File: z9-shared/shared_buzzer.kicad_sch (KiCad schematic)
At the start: 6 parts, among them Q701 AO3400A

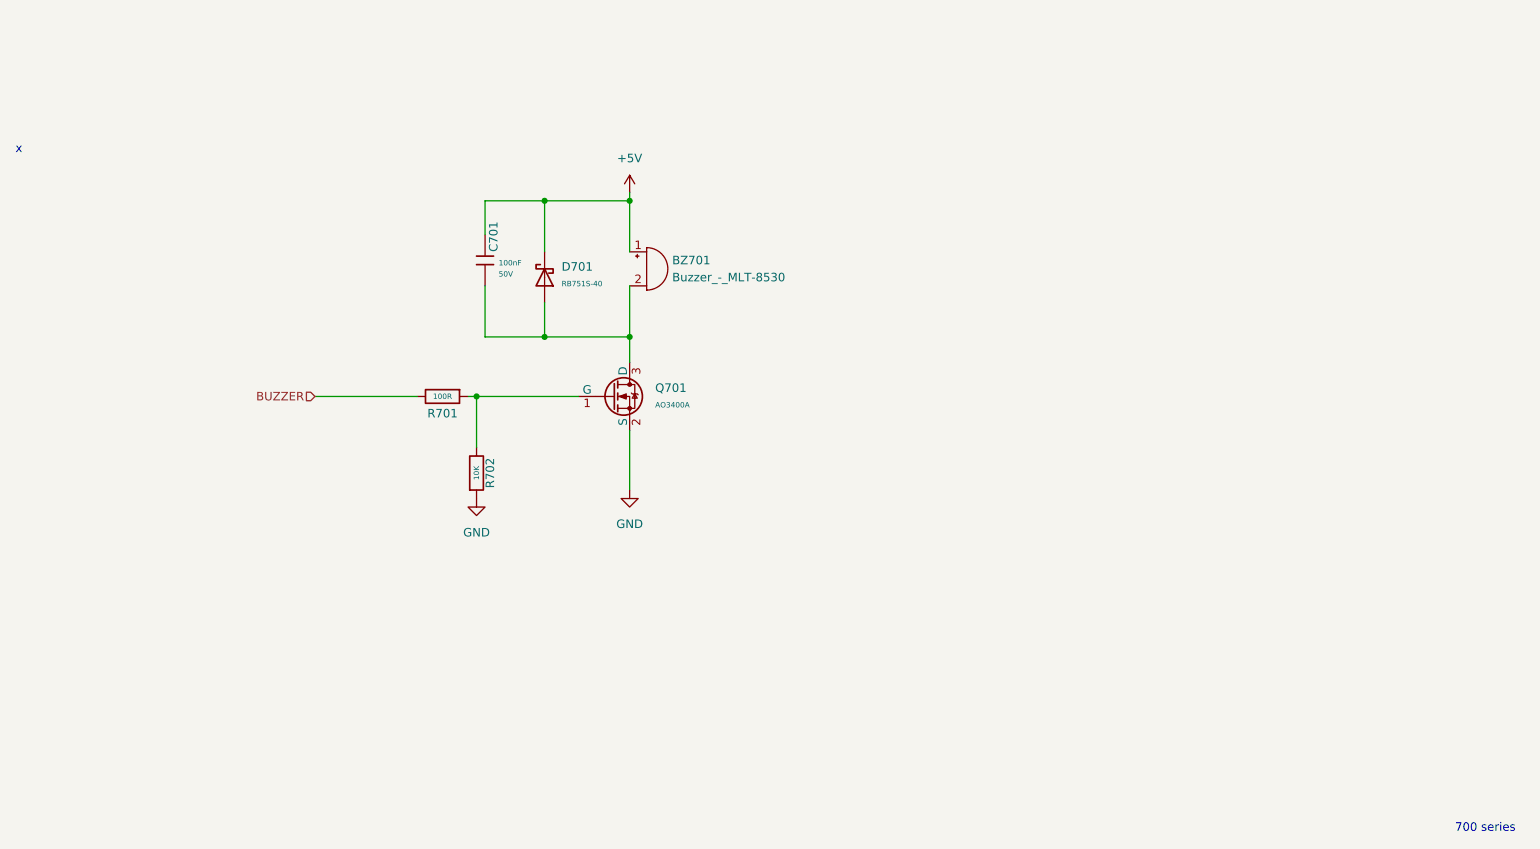
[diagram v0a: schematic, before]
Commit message: Add shared_ism330dhcx schematic and update project configuration - Buzzer chaNGES 3.3v BEADS ANDCAPS - Created a new schematic file for the shared_ism330dhcx component. - Updated the z9-shared project configuration to change the annotation start number from 950 to 700. - Added the shared_ism330dhcx sheet to the main schematic with relevant properties and instances.
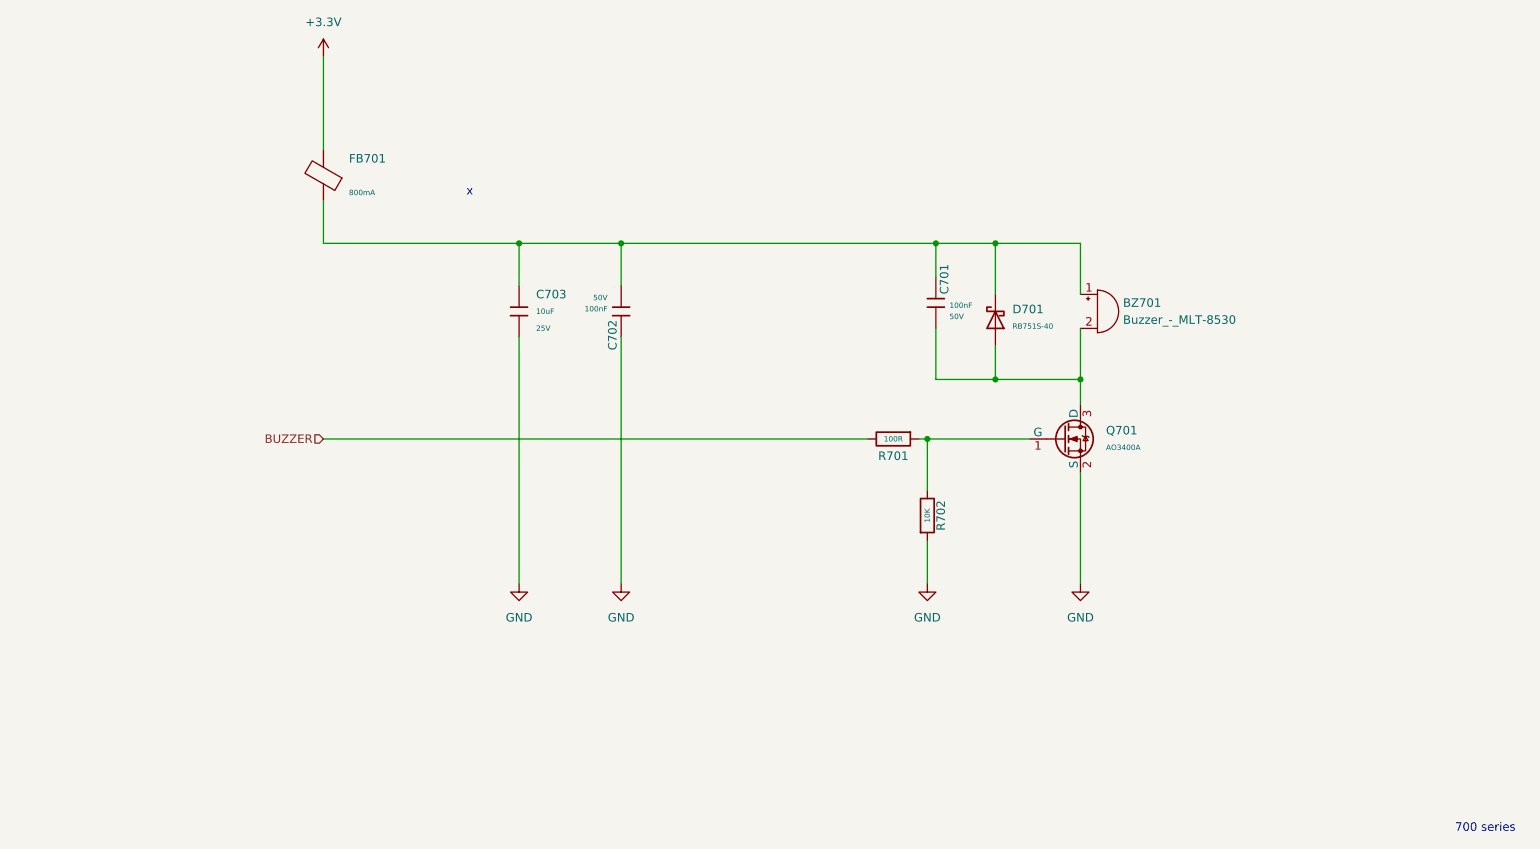
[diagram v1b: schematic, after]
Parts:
- added C702: 100nF, dnt:C_0603_1608Metric, symbol dnt_global:0603,100nF
- added C703: 10uF, dnt:C_0603_1608Metric, symbol dnt_global:0603,10uF,_25V
- added FB701: ~, PCM_JLCPCB:FB_0805, symbol PCM_JLCPCB-Inductors:Ferrite,0805
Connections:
- net GND: now also C702.1, C703.2
- net +5V: no longer names the net of BZ701.1 (+), C701.1, D701.1
- net +5V: now also C702.2, C703.1, FB701.1
- new net +3.3V: FB701.2
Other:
- moved on the sheet: BZ701, C701, D701, Q701, R701, R702

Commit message: fix footprint
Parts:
- FB701: footprint PCM_JLCPCB:FB_0805 -> dnt:F_0805_2012Metric; symbol PCM_JLCPCB-Inductors:Ferrite,0805 -> dnt_global:Ferrite,0805_800mA
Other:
- note removed: "x"
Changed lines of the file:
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@@
 		(comment 1 "Some schematic is shared ")
-	)
-	(text "x"
-		(exclude_from_sim no)
-		(at 125.984 68.58 0)
-		(effects
-			(font
-				(size 1.27 1.27)
-			)
-		)
 	)
 	(text "700 series "
@@
 	)
 	(symbol
-		(lib_id "PCM_JLCPCB-Inductors:Ferrite,0805")
+		(lib_id "dnt_global:Ferrite,0805_800mA")
 		(at 104.14 66.04 180)
 		(unit 1)
@@
 		(fields_autoplaced yes)
 		(property "Reference" "FB701"
-			(at 107.95 63.5507 0)
+			(at 107.95 64.8207 0)
 			(effects
 				(font
@@
 		)
 		(property "Value" "~"
-			(at 107.95 66.0908 0)
+			(at 104.14 66.04 0)
 			(effects
 				(font
 					(size 0.8 0.8)
 				)
-				(justify right)
-			)
-		)
-		(property "Footprint" "PCM_JLCPCB:FB_0805"
+				(justify left)
+			)
+		)
+		(property "Footprint" "dnt:F_0805_2012Metric"
 			(at 105.918 66.04 90)
 			(effects
@@
 		)
 		(property "Current Rating" "800mA"
-			(at 107.95 68.6308 0)
-			(effects
-				(font
+			(at 107.95 67.3608 0)
+			(effects
+				(font

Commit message: Update schematic and project settings for shared components
- Changed the starting annotation number from 700 to 975 in the project configuration.
- Added a new shared schematic sheet named "shared_isolated_can_ps" with relevant properties and instances.
- Included a cautionary text in the schematic to avoid moving components and reannotating to prevent loss of links.
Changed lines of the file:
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@@
 		(fields_autoplaced yes)
 		(property "Reference" "FB701"
-			(at 107.95 64.8207 0)
+			(at 107.95 63.5507 0)
 			(effects
 				(font
@@
 		)
 		(property "Value" "~"
-			(at 104.14 66.04 0)
+			(at 107.95 66.0908 0)
 			(effects
 				(font
 					(size 0.8 0.8)
 				)
-				(justify left)
+				(justify right)
 			)
 		)
@@
 		)
 		(property "Current Rating" "800mA"
-			(at 107.95 67.3608 0)
+			(at 107.95 68.6308 0)
 			(effects
 				(font
@@
 				(path "/09e08bdc-786f-4949-8afc-e02ddbe0502e/1a1ef1d0-80f8-40e1-820b-d8a0de9a6f67"
 					(reference "FB701")
+					(unit 1)
+				)
+			)
+			(project "z9-console"
+				(path "/8d063f79-9282-4820-bcf4-1ff3c006cf08/8d0cf1ff-dd45-490a-9f6d-ad4eb4a5c201"
+					(reference "FB?")
 					(unit 1)
 				)
@@
 				)
 			)
+			(project "z9-console"
+				(path "/8d063f79-9282-4820-bcf4-1ff3c006cf08/8d0cf1ff-dd45-490a-9f6d-ad4eb4a5c201"
+					(reference "#PWR0101")
+					(unit 1)
+				)
+			)
 		)
 	)
@@
 				)
 			)
+			(project "z9-console"
+				(path "/8d063f79-9282-4820-bcf4-1ff3c006cf08/8d0cf1ff-dd45-490a-9f6d-ad4eb4a5c201"
+					(reference "C?")
+					(unit 1)
+				)
+			)
 		)
 	)
@@
 				)
 			)
+			(project "z9-console"
+				(path "/8d063f79-9282-4820-bcf4-1ff3c006cf08/8d0cf1ff-dd45-490a-9f6d-ad4eb4a5c201"
+					(reference "#PWR0102")
+					(unit 1)
+				)
+			)
 		)
 	)
@@
 				)
 			)
+			(project "z9-console"
+				(path "/8d063f79-9282-4820-bcf4-1ff3c006cf08/8d0cf1ff-dd45-490a-9f6d-ad4eb4a5c201"
+					(reference "C?")
+					(unit 1)
+				)
+			)
 		)
 	)
@@
 					(unit 1)
 				)
+			)
+			(project "z9-console"
+				(path "/8d063f79-9282-4820-bcf4-1ff3c006cf08/8d0cf1ff-dd45-490a-9f6d-ad4eb4a5c201"
+					(reference "#PWR0103")
+					(unit 1)
+				)

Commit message: Add z9-console project references and update component properties in shared_buzzer schematic
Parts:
- renumbered C703 to C701, C701 to C703
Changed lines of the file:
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@@
+				)
+			)
+			(project "z9-console"
+				(path "/8d063f79-9282-4820-bcf4-1ff3c006cf08/f06e6e31-c68d-491a-ad1f-dc0bf57e1d1a"
+					(reference "Q701")
+					(unit 1)
 				)
 			)
@@
 				)
 			)
+			(project "z9-console"
+				(path "/8d063f79-9282-4820-bcf4-1ff3c006cf08/f06e6e31-c68d-491a-ad1f-dc0bf57e1d1a"
+					(reference "D701")
+					(unit 1)
+				)
+			)
 			(project "z9-pdm"
 				(path "/b643db5c-578e-4b48-aafc-cc4190db582a/c97401c5-7e03-4d93-a14f-f692468677b5"
@@
 		(dnp no)
 		(fields_autoplaced yes)
-		(property "Reference" "#PWR0704"
+		(property "Reference" "#PWR0702"
 			(at 133.35 133.35 0)
 			(effects
@@
 				(path "/09e08bdc-786f-4949-8afc-e02ddbe0502e/1a1ef1d0-80f8-40e1-820b-d8a0de9a6f67"
 					(reference "#PWR0704")
+					(unit 1)
+				)
+			)
+			(project "z9-console"
+				(path "/8d063f79-9282-4820-bcf4-1ff3c006cf08/f06e6e31-c68d-491a-ad1f-dc0bf57e1d1a"
+					(reference "#PWR0702")
 					(unit 1)
 				)
@@
 		(dnp no)
 		(fields_autoplaced yes)
-		(property "Reference" "#PWR0701"
+		(property "Reference" "#PWR0704"
 			(at 194.31 133.35 0)
 			(effects
@@
 				(path "/09e08bdc-786f-4949-8afc-e02ddbe0502e/1a1ef1d0-80f8-40e1-820b-d8a0de9a6f67"
 					(reference "#PWR0701")
+					(unit 1)
+				)
+			)
+			(project "z9-console"
+				(path "/8d063f79-9282-4820-bcf4-1ff3c006cf08/f06e6e31-c68d-491a-ad1f-dc0bf57e1d1a"
+					(reference "#PWR0704")
 					(unit 1)
 				)
@@
 				)
 			)
+			(project "z9-console"
+				(path "/8d063f79-9282-4820-bcf4-1ff3c006cf08/f06e6e31-c68d-491a-ad1f-dc0bf57e1d1a"
+					(reference "C702")
+					(unit 1)
+				)
+			)
 		)
 	)
@@
 		(on_board yes)
 		(dnp no)
-		(property "Reference" "C701"
+		(property "Reference" "C703"
 			(at 196.85 83.82 90)
 			(effects
@@
 				(path "/09e08bdc-786f-4949-8afc-e02ddbe0502e/1a1ef1d0-80f8-40e1-820b-d8a0de9a6f67"
 					(reference "C701")
+					(unit 1)
+				)
+			)
+			(project "z9-console"
+				(path "/8d063f79-9282-4820-bcf4-1ff3c006cf08/f06e6e31-c68d-491a-ad1f-dc0bf57e1d1a"
+					(reference "C703")
 					(unit 1)
 				)
@@
 				)
 			)
+			(project "z9-console"
+				(path "/8d063f79-9282-4820-bcf4-1ff3c006cf08/f06e6e31-c68d-491a-ad1f-dc0bf57e1d1a"
+					(reference "BZ701")
+					(unit 1)
+				)
+			)
 			(project "z9-pdm"
 				(path "/b643db5c-578e-4b48-aafc-cc4190db582a/c97401c5-7e03-4d93-a14f-f692468677b5"
@@
 		(dnp no)
 		(fields_autoplaced yes)
-		(property "Reference" "#PWR0702"
+		(property "Reference" "#PWR0703"
 			(at 148.59 133.35 0)
 			(effects
@@
 				(path "/09e08bdc-786f-4949-8afc-e02ddbe0502e/1a1ef1d0-80f8-40e1-820b-d8a0de9a6f67"
 					(reference "#PWR0702")
+					(unit 1)
+				)
+			)
+			(project "z9-console"
+				(path "/8d063f79-9282-4820-bcf4-1ff3c006cf08/f06e6e31-c68d-491a-ad1f-dc0bf57e1d1a"
+					(reference "#PWR0703")
 					(unit 1)
 				)
@@
 		(dnp no)
 		(fields_autoplaced yes)
-		(property "Reference" "C703"
+		(property "Reference" "C701"
 			(at 135.89 83.8199 0)
 			(effects
@@
 			(project ""
 				(path "/8d063f79-9282-4820-bcf4-1ff3c006cf08/f06e6e31-c68d-491a-ad1f-dc0bf57e1d1a"
-					(reference "C703")
+					(reference "C701")
 					(unit 1)
 				)
@@
 				)
 			)
+			(project "z9-console"
+				(path "/8d063f79-9282-4820-bcf4-1ff3c006cf08/f06e6e31-c68d-491a-ad1f-dc0bf57e1d1a"
+					(reference "R702")
+					(unit 1)
+				)
+			)
 			(project "z9-pdm"
 				(path "/b643db5c-578e-4b48-aafc-cc4190db582a/c97401c5-7e03-4d93-a14f-f692468677b5"
@@
 		(dnp no)
 		(fields_autoplaced yes)
-		(property "Reference" "#PWR0953"
+		(property "Reference" "#PWR0701"
 			(at 104.14 52.07 0)
 			(effects
@@
 			(project ""
 				(path "/8d063f79-9282-4820-bcf4-1ff3c006cf08/f06e6e31-c68d-491a-ad1f-dc0bf57e1d1a"
-					(reference "#PWR0953")
+					(reference "#PWR0701")
 					(unit 1)
 				)
@@
 				)
 			)
+			(project "z9-console"
+				(path "/8d063f79-9282-4820-bcf4-1ff3c006cf08/f06e6e31-c68d-491a-ad1f-dc0bf57e1d1a"
+					(reference "R701")
+					(unit 1)
+				)
+			)
 			(project "z9-pdm"
 				(path "/b643db5c-578e-4b48-aafc-cc4190db582a/c97401c5-7e03-4d93-a14f-f692468677b5"
@@
 		(dnp no)
 		(fields_autoplaced yes)
-		(property "Reference" "#PWR0703"
+		(property "Reference" "#PWR0705"
 			(at 217.17 133.35 0)
 			(effects
@@
 					(unit 1)
 				)
+			)
+			(project "z9-console"
+				(path "/8d063f79-9282-4820-bcf4-1ff3c006cf08/f06e6e31-c68d-491a-ad1f-dc0bf57e1d1a"
+					(reference "#PWR0705")
+					(unit 1)
+				)

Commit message: x
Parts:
- renumbered C703 to C701, C701 to C703
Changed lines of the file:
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@@
 		(instances
 			(project ""
-				(path "/09e08bdc-786f-4949-8afc-e02ddbe0502e/1a1ef1d0-80f8-40e1-820b-d8a0de9a6f67"
+				(path "/09e08bdc-786f-4949-8afc-e02ddbe0502e/4ba7270b-fda7-4f09-aaf0-2021d0ea5e88"
 					(reference "FB701")
 					(unit 1)
@@
 		(instances
 			(project "z9-shared"
-				(path "/09e08bdc-786f-4949-8afc-e02ddbe0502e/1a1ef1d0-80f8-40e1-820b-d8a0de9a6f67"
+				(path "/09e08bdc-786f-4949-8afc-e02ddbe0502e/4ba7270b-fda7-4f09-aaf0-2021d0ea5e88"
 					(reference "Q701")
 					(unit 1)
@@
 		(instances
 			(project "z9-shared"
-				(path "/09e08bdc-786f-4949-8afc-e02ddbe0502e/1a1ef1d0-80f8-40e1-820b-d8a0de9a6f67"
+				(path "/09e08bdc-786f-4949-8afc-e02ddbe0502e/4ba7270b-fda7-4f09-aaf0-2021d0ea5e88"
 					(reference "D701")
 					(unit 1)
@@
 		(dnp no)
 		(fields_autoplaced yes)
-		(property "Reference" "#PWR0702"
+		(property "Reference" "#PWR0704"
 			(at 133.35 133.35 0)
 			(effects
@@
 		(instances
 			(project "z9-shared"
-				(path "/09e08bdc-786f-4949-8afc-e02ddbe0502e/1a1ef1d0-80f8-40e1-820b-d8a0de9a6f67"
+				(path "/09e08bdc-786f-4949-8afc-e02ddbe0502e/4ba7270b-fda7-4f09-aaf0-2021d0ea5e88"
 					(reference "#PWR0704")
 					(unit 1)
@@
 		(dnp no)
 		(fields_autoplaced yes)
-		(property "Reference" "#PWR0704"
+		(property "Reference" "#PWR0701"
 			(at 194.31 133.35 0)
 			(effects
@@
 		(instances
 			(project "z9-shared"
-				(path "/09e08bdc-786f-4949-8afc-e02ddbe0502e/1a1ef1d0-80f8-40e1-820b-d8a0de9a6f67"
+				(path "/09e08bdc-786f-4949-8afc-e02ddbe0502e/4ba7270b-fda7-4f09-aaf0-2021d0ea5e88"
 					(reference "#PWR0701")
 					(unit 1)
@@
 		(instances
 			(project "z9-shared"
-				(path "/09e08bdc-786f-4949-8afc-e02ddbe0502e/1a1ef1d0-80f8-40e1-820b-d8a0de9a6f67"
+				(path "/09e08bdc-786f-4949-8afc-e02ddbe0502e/4ba7270b-fda7-4f09-aaf0-2021d0ea5e88"
 					(reference "C702")
 					(unit 1)
@@
 		(on_board yes)
 		(dnp no)
-		(property "Reference" "C703"
+		(property "Reference" "C701"
 			(at 196.85 83.82 90)
 			(effects
@@
 		(instances
 			(project "z9-shared"
-				(path "/09e08bdc-786f-4949-8afc-e02ddbe0502e/1a1ef1d0-80f8-40e1-820b-d8a0de9a6f67"
+				(path "/09e08bdc-786f-4949-8afc-e02ddbe0502e/4ba7270b-fda7-4f09-aaf0-2021d0ea5e88"
 					(reference "C701")
 					(unit 1)
@@
 		(instances
 			(project "z9-shared"
-				(path "/09e08bdc-786f-4949-8afc-e02ddbe0502e/1a1ef1d0-80f8-40e1-820b-d8a0de9a6f67"
+				(path "/09e08bdc-786f-4949-8afc-e02ddbe0502e/4ba7270b-fda7-4f09-aaf0-2021d0ea5e88"
 					(reference "BZ701")
 					(unit 1)
@@
 		(dnp no)
 		(fields_autoplaced yes)
-		(property "Reference" "#PWR0703"
+		(property "Reference" "#PWR0702"
 			(at 148.59 133.35 0)
 			(effects
@@
 		(instances
 			(project "z9-shared"
-				(path "/09e08bdc-786f-4949-8afc-e02ddbe0502e/1a1ef1d0-80f8-40e1-820b-d8a0de9a6f67"
+				(path "/09e08bdc-786f-4949-8afc-e02ddbe0502e/4ba7270b-fda7-4f09-aaf0-2021d0ea5e88"
 					(reference "#PWR0702")
 					(unit 1)
@@
 		(dnp no)
 		(fields_autoplaced yes)
-		(property "Reference" "C701"
+		(property "Reference" "C703"
 			(at 135.89 83.8199 0)
 			(effects
@@
 		(instances
 			(project ""
-				(path "/09e08bdc-786f-4949-8afc-e02ddbe0502e/1a1ef1d0-80f8-40e1-820b-d8a0de9a6f67"
+				(path "/09e08bdc-786f-4949-8afc-e02ddbe0502e/4ba7270b-fda7-4f09-aaf0-2021d0ea5e88"
 					(reference "C703")
 					(unit 1)
@@
 		(instances
 			(project "z9-shared"
-				(path "/09e08bdc-786f-4949-8afc-e02ddbe0502e/1a1ef1d0-80f8-40e1-820b-d8a0de9a6f67"
+				(path "/09e08bdc-786f-4949-8afc-e02ddbe0502e/4ba7270b-fda7-4f09-aaf0-2021d0ea5e88"
 					(reference "R702")
 					(unit 1)
@@
 		(dnp no)
 		(fields_autoplaced yes)
-		(property "Reference" "#PWR0701"
+		(property "Reference" "#PWR0953"
 			(at 104.14 52.07 0)
 			(effects
@@
 		(instances
 			(project ""
-				(path "/09e08bdc-786f-4949-8afc-e02ddbe0502e/1a1ef1d0-80f8-40e1-820b-d8a0de9a6f67"
+				(path "/09e08bdc-786f-4949-8afc-e02ddbe0502e/4ba7270b-fda7-4f09-aaf0-2021d0ea5e88"
 					(reference "#PWR0953")
 					(unit 1)
@@
 		(instances
 			(project "z9-shared"
-				(path "/09e08bdc-786f-4949-8afc-e02ddbe0502e/1a1ef1d0-80f8-40e1-820b-d8a0de9a6f67"
+				(path "/09e08bdc-786f-4949-8afc-e02ddbe0502e/4ba7270b-fda7-4f09-aaf0-2021d0ea5e88"
 					(reference "R701")
 					(unit 1)
@@
 		(dnp no)
 		(fields_autoplaced yes)
-		(property "Reference" "#PWR0705"
+		(property "Reference" "#PWR0703"
 			(at 217.17 133.35 0)
 			(effects
@@
 		(instances
 			(project "z9-shared"
-				(path "/09e08bdc-786f-4949-8afc-e02ddbe0502e/1a1ef1d0-80f8-40e1-820b-d8a0de9a6f67"
+				(path "/09e08bdc-786f-4949-8afc-e02ddbe0502e/4ba7270b-fda7-4f09-aaf0-2021d0ea5e88"
 					(reference "#PWR0703")
 					(unit 1)

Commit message: x
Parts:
- renumbered C703 to C701, C701 to C703
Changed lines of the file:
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@@
 		(dnp no)
 		(fields_autoplaced yes)
-		(property "Reference" "#PWR0704"
+		(property "Reference" "#PWR0702"
 			(at 133.35 133.35 0)
 			(effects
@@
 		(dnp no)
 		(fields_autoplaced yes)
-		(property "Reference" "#PWR0701"
+		(property "Reference" "#PWR0704"
 			(at 194.31 133.35 0)
 			(effects
@@
 		(on_board yes)
 		(dnp no)
-		(property "Reference" "C701"
+		(property "Reference" "C703"
 			(at 196.85 83.82 90)
 			(effects
@@
 		(dnp no)
 		(fields_autoplaced yes)
-		(property "Reference" "#PWR0702"
+		(property "Reference" "#PWR0703"
 			(at 148.59 133.35 0)
 			(effects
@@
 		(dnp no)
 		(fields_autoplaced yes)
-		(property "Reference" "C703"
+		(property "Reference" "C701"
 			(at 135.89 83.8199 0)
 			(effects
@@
 		(dnp no)
 		(fields_autoplaced yes)
-		(property "Reference" "#PWR0953"
+		(property "Reference" "#PWR0701"
 			(at 104.14 52.07 0)
 			(effects
@@
 		(dnp no)
 		(fields_autoplaced yes)
-		(property "Reference" "#PWR0703"
+		(property "Reference" "#PWR0705"
 			(at 217.17 133.35 0)
 			(effects
